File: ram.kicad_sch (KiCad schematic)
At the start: 44 parts, among them IC5 MT41K256M16TW-107_P

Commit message: first power management layout iteration, added footprints and values to parts that had none
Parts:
- removed IC5: MT41K256M16TW-107_P, ARMband:BGA96C80P9X16_800X1400X120, symbol ARMband:MT41K256M16TW-107_P
- added IC2: MT41K256M16TW-107_P, ARMband:BGA96C80P9X16_800X1400X120, symbol ARMband:MT41K256M16TW-107_P
- C52, C53, C54, C55, C56, C57, C58, C59, C60, C61, C62, C63, C64, C65: footprint (none) -> Capacitor_SMD:C_0402_1005Metric
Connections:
- net DDR_A0: now also IC2.N3 (A0)
- net DDR_A1: now also IC2.P7 (A1)
- net DDR_A10: now also IC2.L7 (A10/AP)
- net DDR_A11: now also IC2.R7 (A11)
- net DDR_A12: now also IC2.N7 (A12/BC#)
- net DDR_A13: now also IC2.T3 (A13)
- net DDR_A14: now also IC2.T7 (A14)
- net DDR_A2: now also IC2.P3 (A2)
- net DDR_A3: now also IC2.N2 (A3)
- net DDR_A4: now also IC2.P8 (A4)
- net DDR_A5: now also IC2.P2 (A5)
- net DDR_A6: now also IC2.R8 (A6)
- net DDR_A7: now also IC2.R2 (A7)
- net DDR_A8: now also IC2.T8 (A8)
- net DDR_A9: now also IC2.R3 (A9)
- net DDR_BA0: now also IC2.M2 (BA0)
- net DDR_BA1: now also IC2.N8 (BA1)
- net DDR_BA2: now also IC2.M3 (BA2)
- net DDR_CASN: now also IC2.K3 (CAS#)
- net DDR_CKE: now also IC2.K9 (CKE)
- net DDR_CLK_N: now also IC2.K7 (CK#)
- net DDR_CLK_P: now also IC2.J7 (CK)
- net DDR_CSN: now also IC2.L2 (CS#)
- net DDR_DQ0: now also IC2.E3 (DQ0)
- net DDR_DQ1: now also IC2.F7 (DQ1)
- net DDR_DQ10: now also IC2.C8 (DQ10)
- net DDR_DQ11: now also IC2.C2 (DQ11)
- net DDR_DQ12: now also IC2.A7 (DQ12)
- net DDR_DQ13: now also IC2.A2 (DQ13)
- net DDR_DQ14: now also IC2.B8 (DQ14)
- net DDR_DQ15: now also IC2.A3 (DQ15)
- net DDR_DQ2: now also IC2.F2 (DQ2)
- net DDR_DQ3: now also IC2.F8 (DQ3)
- net DDR_DQ4: now also IC2.H3 (DQ4)
- net DDR_DQ5: now also IC2.H8 (DQ5)
- net DDR_DQ6: now also IC2.G2 (DQ6)
- net DDR_DQ7: now also IC2.H7 (DQ7)
- net DDR_DQ8: now also IC2.D7 (DQ8)
- net DDR_DQ9: now also IC2.C3 (DQ9)
- net DDR_DQM0: now also IC2.D3 (UDM)
- net DDR_DQM1: now also IC2.E7 (LDM)
- net DDR_DQS0_N: now also IC2.B7 (UDQS#)
- net DDR_DQS0_P: now also IC2.C7 (UDQS)
- net DDR_DQSI_N: now also IC2.F3 (LDQS)
- net DDR_DQSI_P: now also IC2.G3 (LDQS#)
- net DDR_ODT: now also IC2.L8 (ZQ)
- net DDR_RASN: now also IC2.J3 (RAS#)
- net DDR_RESETN: now also IC2.T2 (RESET#)
- net DDR_WEN: now also IC2.L3 (WE#)
- net DDR_ZQ: now also IC2.K1 (ODT)

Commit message: Add missing footprints to components
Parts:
- R40, R41: footprint (none) -> Resistor_SMD:R_0402_1005Metric
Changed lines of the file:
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@@
       (effects (font (size 1.27 1.27)))
     )
-    (property "Footprint" "" (at 144.78 41.91 0)
+    (property "Footprint" "Resistor_SMD:R_0402_1005Metric" (at 144.78 41.91 0)
       (effects (font (size 1.27 1.27)) hide)
     )
@@
       (effects (font (size 1.27 1.27)))
     )
-    (property "Footprint" "" (at 144.78 30.48 0)
+    (property "Footprint" "Resistor_SMD:R_0402_1005Metric" (at 144.78 30.48 0)
       (effects (font (size 1.27 1.27)) hide)
     )

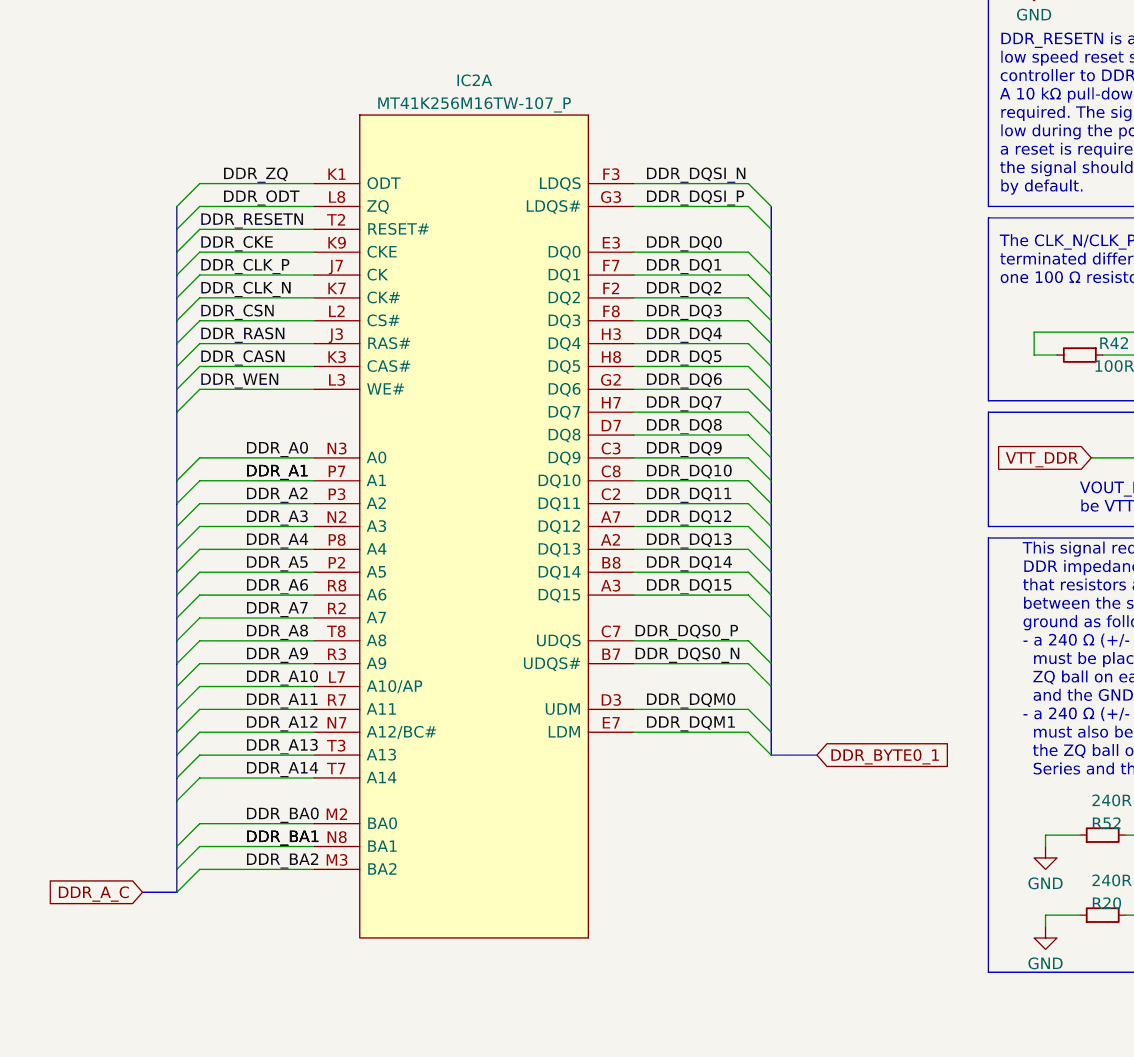
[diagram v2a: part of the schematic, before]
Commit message: Update local symbols for DDR Pins to global
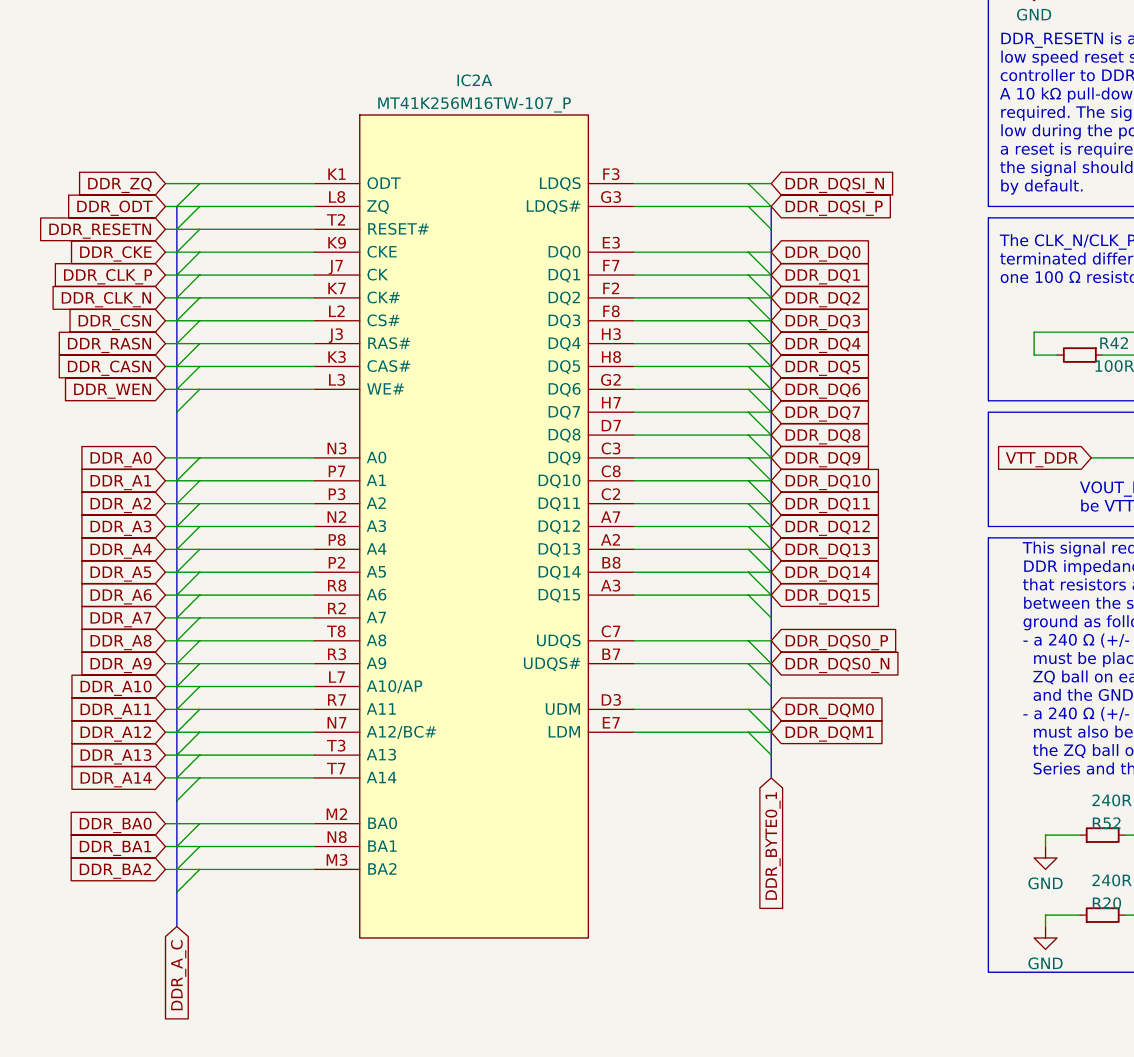
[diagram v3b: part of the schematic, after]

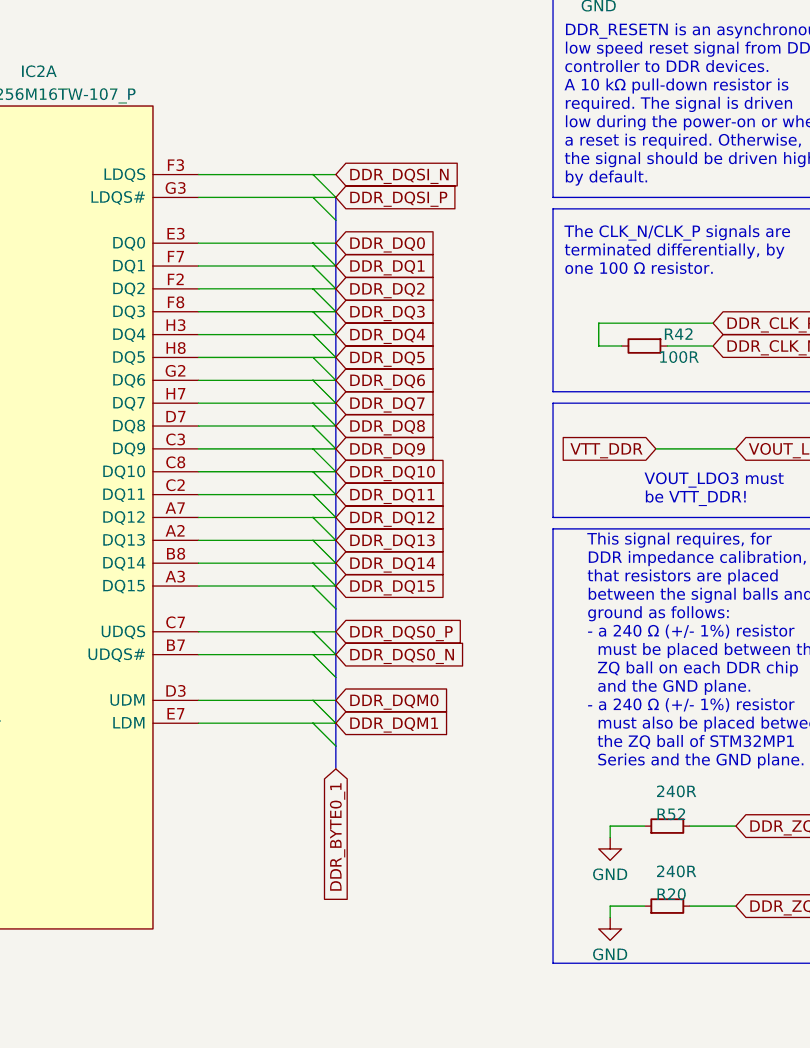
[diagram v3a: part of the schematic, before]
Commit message: reworked RAM
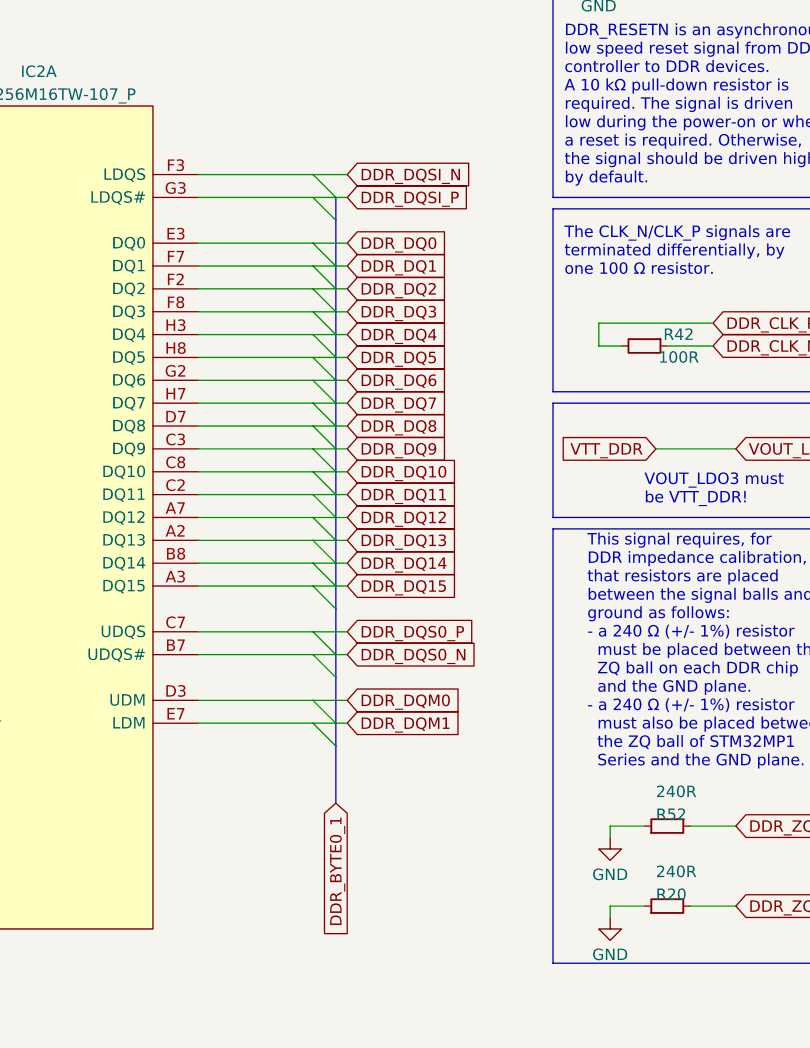
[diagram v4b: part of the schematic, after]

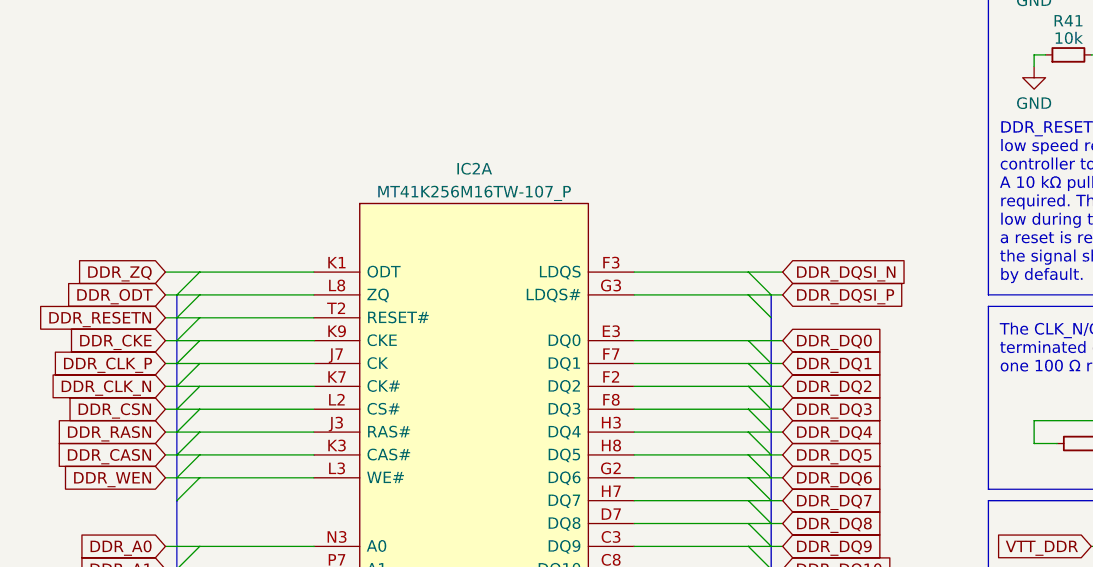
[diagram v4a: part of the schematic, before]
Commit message: Fix RAM Labels
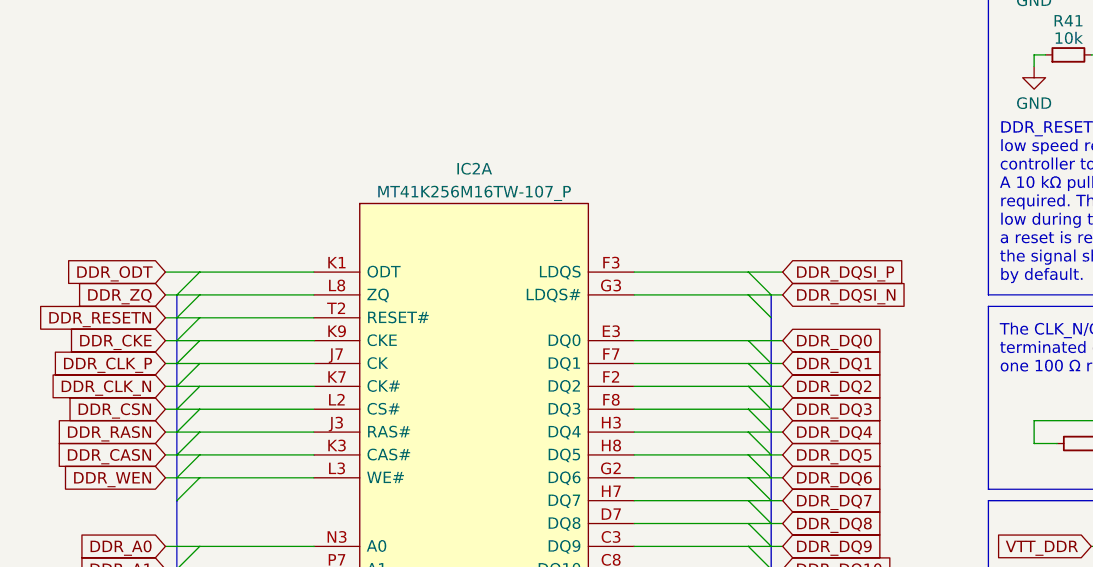
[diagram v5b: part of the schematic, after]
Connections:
- net DDR_DQSI_N: now also IC2.G3 (LDQS#); no longer IC2.F3 (LDQS)
- net DDR_DQSI_P: now also IC2.F3 (LDQS); no longer IC2.G3 (LDQS#)
- net DDR_ODT: now also IC2.K1 (ODT); no longer IC2.L8 (ZQ)
- net DDR_ZQ: now also IC2.L8 (ZQ); no longer IC2.K1 (ODT)
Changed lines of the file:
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@@
+    )
+  )
+  (global_label "DDR_ZQ" (shape input) (at 44.45 68.58 180) (fields_autoplaced)
+    (effects (font (size 1.27 1.27)) (justify right))
+    (property "Intersheetrefs" "${INTERSHEET_REFS}" (at 0 2.54 0)
+      (effects (font (size 1.27 1.27)) hide)
     )
   )
@@
     (effects (font (size 1.27 1.27)) (justify right))
     (property "Intersheetrefs" "${INTERSHEET_REFS}" (at 0 0 0)
+      (effects (font (size 1.27 1.27)) hide)
+    )
+  )
+  (global_label "DDR_DQSI_P" (shape input) (at 113.03 66.04 0) (fields_autoplaced)
+    (effects (font (size 1.27 1.27)) (justify left))
+    (property "Intersheetrefs" "${INTERSHEET_REFS}" (at 1.27 -2.54 0)
       (effects (font (size 1.27 1.27)) hide)
     )
@@
     )
   )
-  (global_label "DDR_ODT" (shape input) (at 44.45 68.58 180) (fields_autoplaced)
-    (effects (font (size 1.27 1.27)) (justify right))
-    (property "Intersheetrefs" "${INTERSHEET_REFS}" (at 0 0 0)
-      (effects (font (size 1.27 1.27)) hide)
-    )
-  )
   (global_label "DDR_A12" (shape input) (at 44.45 127 180) (fields_autoplaced)
     (effects (font (size 1.27 1.27)) (justify right))
@@
     )
   )
-  (global_label "DDR_DQSI_P" (shape input) (at 113.03 68.58 0) (fields_autoplaced)
-    (effects (font (size 1.27 1.27)) (justify left))
-    (property "Intersheetrefs" "${INTERSHEET_REFS}" (at 1.27 0 0)
-      (effects (font (size 1.27 1.27)) hide)
-    )
-  )
   (global_label "DDR_A2" (shape input) (at 44.45 101.6 180) (fields_autoplaced)
     (effects (font (size 1.27 1.27)) (justify right))
@@
     )
   )
+  (global_label "DDR_ODT" (shape input) (at 44.45 66.04 180) (fields_autoplaced)
+    (effects (font (size 1.27 1.27)) (justify right))
+    (property "Intersheetrefs" "${INTERSHEET_REFS}" (at 0 -2.54 0)
+      (effects (font (size 1.27 1.27)) hide)
+    )
+  )
   (global_label "DDR_DQ14" (shape input) (at 113.03 109.22 0) (fields_autoplaced)
     (effects (font (size 1.27 1.27)) (justify left))
@@
     )
   )
+  (global_label "DDR_DQSI_N" (shape input) (at 113.03 68.58 0) (fields_autoplaced)
+    (effects (font (size 1.27 1.27)) (justify left))
+    (property "Intersheetrefs" "${INTERSHEET_REFS}" (at 1.27 2.54 0)
+      (effects (font (size 1.27 1.27)) hide)
+    )
+  )
   (global_label "DDR_CSN" (shape input) (at 44.45 81.28 180) (fields_autoplaced)
     (effects (font (size 1.27 1.27)) (justify right))
@@
     (effects (font (size 1.27 1.27)) (justify right))
     (property "Intersheetrefs" "${INTERSHEET_REFS}" (at 0 0 0)
-      (effects (font (size 1.27 1.27)) hide)
-    )
-  )
-  (global_label "DDR_DQSI_N" (shape input) (at 113.03 66.04 0) (fields_autoplaced)
-    (effects (font (size 1.27 1.27)) (justify left))
-    (property "Intersheetrefs" "${INTERSHEET_REFS}" (at 1.27 0 0)
-      (effects (font (size 1.27 1.27)) hide)
-    )
-  )
-  (global_label "DDR_ZQ" (shape input) (at 44.45 66.04 180) (fields_autoplaced)
-    (effects (font (size 1.27 1.27)) (justify right))
-    (property "Intersheetrefs" "${INTERSHEET_REFS}" (at 0 0 0)
